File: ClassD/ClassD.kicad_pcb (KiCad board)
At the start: 2 copper layers, 53 parts, among them P1 RedRCA, P2 WhiteRCA, P3 CONN_01X02, P4 CONN_01X02, P5 CONN_01X02, SW1 SW_PUSH, SW2 SW_PUSH, U1 TDA7491LP, U2 MCP1700T

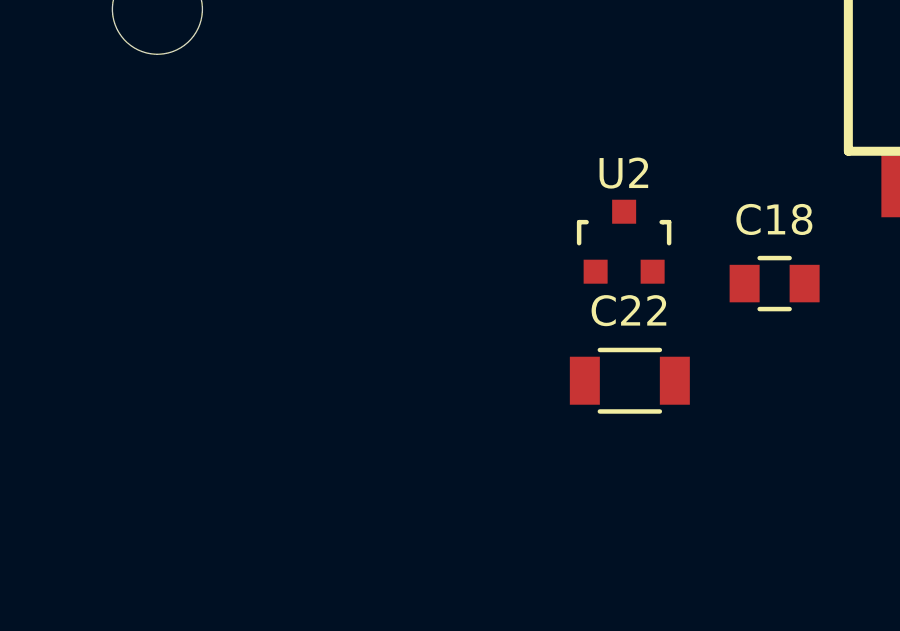
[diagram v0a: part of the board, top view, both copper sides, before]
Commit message: Added power indicator LED
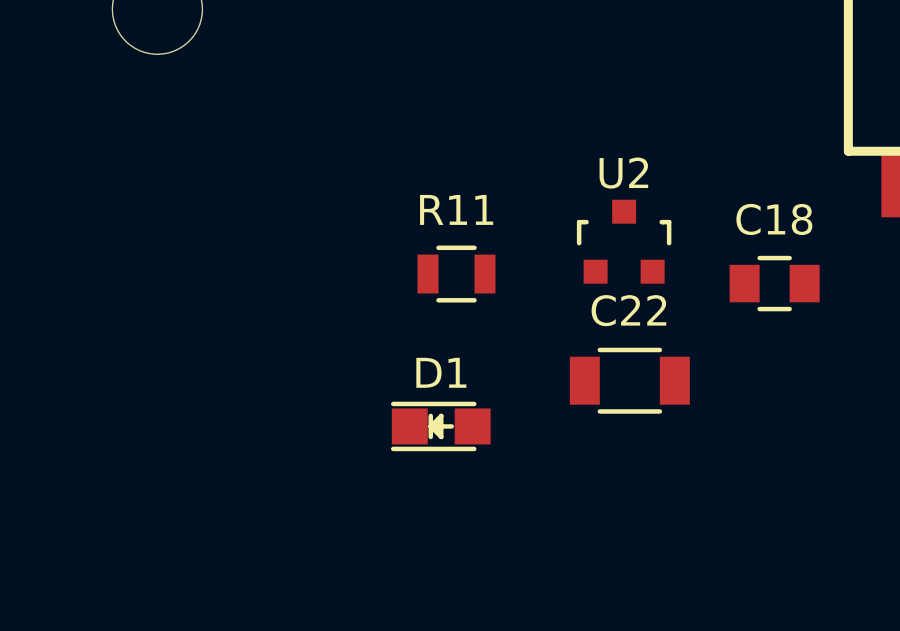
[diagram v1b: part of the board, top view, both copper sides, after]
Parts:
- added D1: LED, LEDs:LED_0805, F.Cu at (140.7, 160.4)
- added R11: 499, Resistors_SMD:R_0805, F.Cu at (141.2, 155.3)
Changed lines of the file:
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@@
 (kicad_pcb (version 4) (host pcbnew 4.0.1-3.201512221402+6198~38~ubuntu14.04.1-stable)
   (general
-    (links 110)
-    (no_connects 110)
-    (area 0 0 0 0)
+    (links 113)
+    (no_connects 113)
+    (area -2.125001 -3.225 273.562881 166.4065)
     (thickness 1.6)
     (drawings 0)
     (tracks 0)
     (zones 0)
-    (modules 53)
-    (nets 39)
+    (modules 55)
+    (nets 40)
   )
   (page A4)
@@
   (net 37 "Net-(R7-Pad2)")
   (net 38 "Net-(R8-Pad2)")
+  (net 39 "Net-(D1-Pad1)")
   (net_class Default "This is the default net class."
     (clearance 0.2)
@@
     (add_net "Net-(C6-Pad1)")
     (add_net "Net-(C9-Pad2)")
+    (add_net "Net-(D1-Pad1)")
     (add_net "Net-(L1-Pad2)")
     (add_net "Net-(L3-Pad2)")
@@
       (at (xyz 0 0 0))
       (scale (xyz 1 1 1))
+      (rotate (xyz 0 0 0))
+    )
+  )
+  (module LEDs:LED_0805 (layer F.Cu)
+    (at 140.6525 160.401)
+    (descr "LED 0805 smd package")
+    (tags "LED 0805 SMD")
+    (attr smd)
+    (fp_text reference D1 (at 0 -1.75) (layer F.SilkS)
+      (effects (font (size 1 1) (thickness 0.15)))
+    )
+    (fp_text value LED (at 0 1.75) (layer F.Fab)
+      (effects (font (size 1 1) (thickness 0.15)))
+    )
+    (fp_line (start -1.6 0.75) (end 1.1 0.75) (layer F.SilkS) (width 0.15))
+    (fp_line (start -1.6 -0.75) (end 1.1 -0.75) (layer F.SilkS) (width 0.15))
+    (fp_line (start -0.1 0.15) (end -0.1 -0.1) (layer F.SilkS) (width 0.15))
+    (fp_line (start -0.1 -0.1) (end -0.25 0.05) (layer F.SilkS) (width 0.15))
+    (fp_line (start -0.35 -0.35) (end -0.35 0.35) (layer F.SilkS) (width 0.15))
+    (fp_line (start 0 0) (end 0.35 0) (layer F.SilkS) (width 0.15))
+    (fp_line (start -0.35 0) (end 0 -0.35) (layer F.SilkS) (width 0.15))
+    (fp_line (start 0 -0.35) (end 0 0.35) (layer F.SilkS) (width 0.15))
+    (fp_line (start 0 0.35) (end -0.35 0) (layer F.SilkS) (width 0.15))
+    (fp_line (start 1.9 -0.95) (end 1.9 0.95) (layer F.CrtYd) (width 0.05))
+    (fp_line (start 1.9 0.95) (end -1.9 0.95) (layer F.CrtYd) (width 0.05))
+    (fp_line (start -1.9 0.95) (end -1.9 -0.95) (layer F.CrtYd) (width 0.05))
+    (fp_line (start -1.9 -0.95) (end 1.9 -0.95) (layer F.CrtYd) (width 0.05))
+    (pad 2 smd rect (at 1.04902 0 180) (size 1.19888 1.19888) (layers F.Cu F.Paste F.Mask)
+      (net 26 /3V3))
+    (pad 1 smd rect (at -1.04902 0 180) (size 1.19888 1.19888) (layers F.Cu F.Paste F.Mask)
+      (net 39 "Net-(D1-Pad1)"))
+    (model LEDs.3dshapes/LED_0805.wrl
+      (at (xyz 0 0 0))
+      (scale (xyz 1 1 1))
+      (rotate (xyz 0 0 0))
+    )
+  )
+  (module Resistors_SMD:R_0805 (layer F.Cu)
+    (at 141.1605 155.321)
+    (descr "Resistor SMD 0805, reflow soldering, Vishay (see dcrcw.pdf)")
+    (tags "resistor 0805")
+    (attr smd)
+    (fp_text reference R11 (at 0 -2.1) (layer F.SilkS)
+      (effects (font (size 1 1) (thickness 0.15)))
+    )
+    (fp_text value 499 (at 0 2.1) (layer F.Fab)
+      (effects (font (size 1 1) (thickness 0.15)))
+    )
+    (fp_line (start -1.6 -1) (end 1.6 -1) (layer F.CrtYd) (width 0.05))
+    (fp_line (start -1.6 1) (end 1.6 1) (layer F.CrtYd) (width 0.05))
+    (fp_line (start -1.6 -1) (end -1.6 1) (layer F.CrtYd) (width 0.05))
+    (fp_line (start 1.6 -1) (end 1.6 1) (layer F.CrtYd) (width 0.05))
+    (fp_line (start 0.6 0.875) (end -0.6 0.875) (layer F.SilkS) (width 0.15))
+    (fp_line (start -0.6 -0.875) (end 0.6 -0.875) (layer F.SilkS) (width 0.15))
+    (pad 1 smd rect (at -0.95 0) (size 0.7 1.3) (layers F.Cu F.Paste F.Mask)
+      (net 39 "Net-(D1-Pad1)"))
+    (pad 2 smd rect (at 0.95 0) (size 0.7 1.3) (layers F.Cu F.Paste F.Mask)
+      (net 5 OGND))
+    (model Resistors_SMD.3dshapes/R_0805.wrl
+      (at (xyz 0 0 0))
+      (scale (xyz 1 1 1))

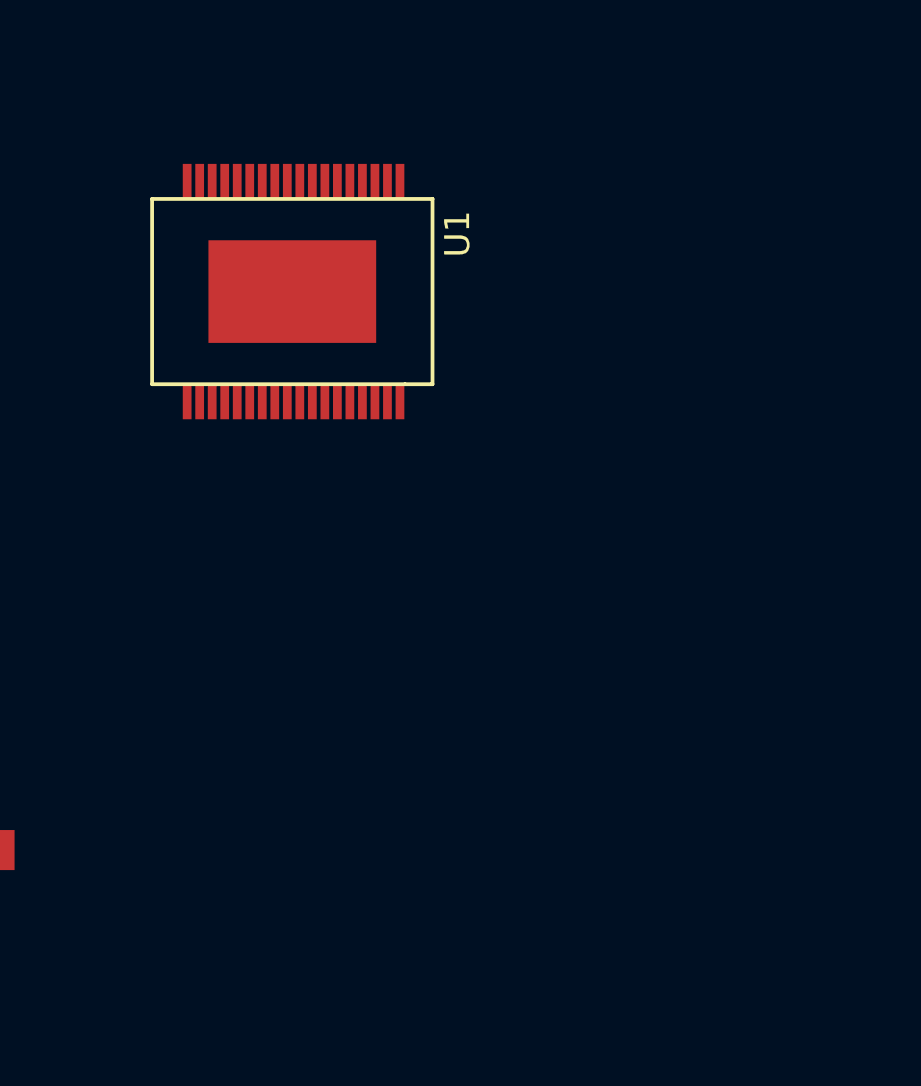
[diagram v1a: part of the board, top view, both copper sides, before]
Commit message: Added ferrites, finished component grouping
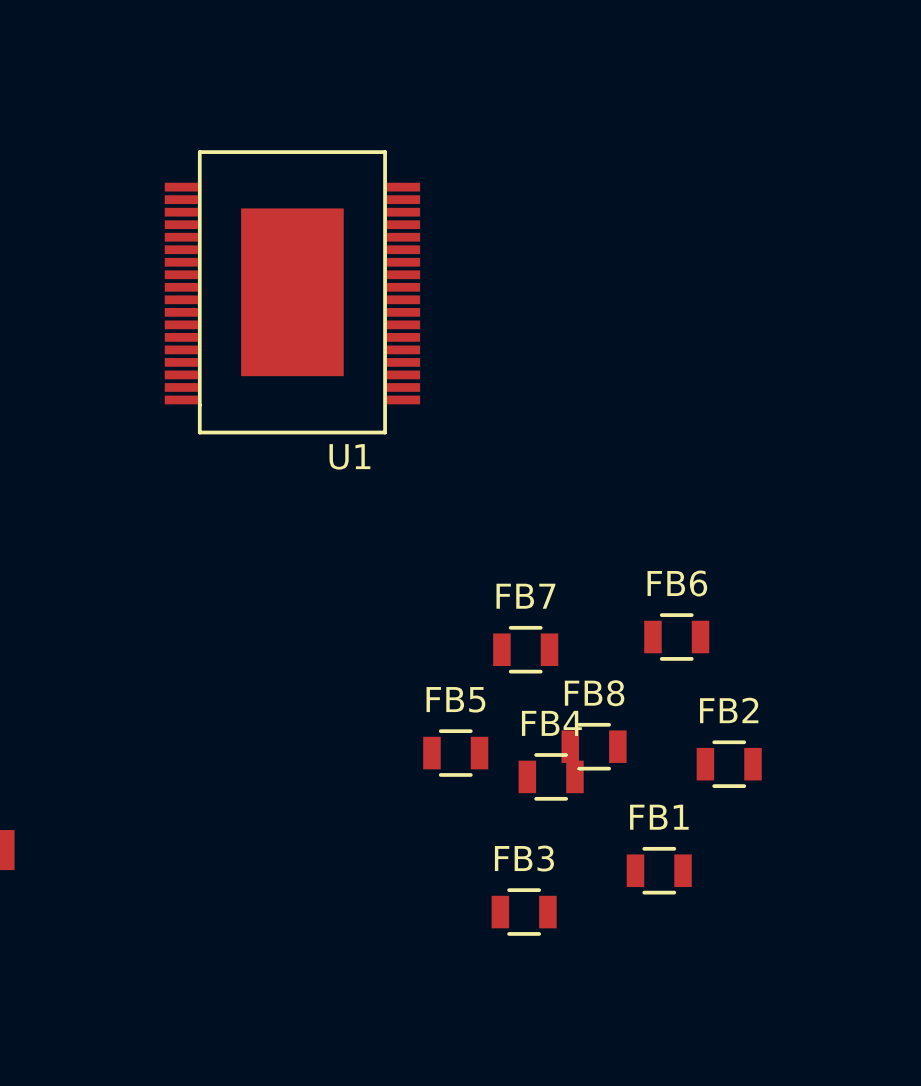
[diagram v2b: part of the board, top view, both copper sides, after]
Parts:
- added FB1: Ferrite, Resistors_SMD:R_0805, F.Cu at (193.6, 140.3)
- added FB2: Ferrite, Resistors_SMD:R_0805, F.Cu at (196.4, 136.0)
- added FB3: Ferrite, Resistors_SMD:R_0805, F.Cu at (188.2, 141.9)
- added FB4: Ferrite, Resistors_SMD:R_0805, F.Cu at (189.3, 136.5)
- added FB5: Ferrite, Resistors_SMD:R_0805, F.Cu at (185.5, 135.6)
- added FB6: Ferrite, Resistors_SMD:R_0805, F.Cu at (194.3, 130.9)
- added FB7: Ferrite, Resistors_SMD:R_0805, F.Cu at (188.3, 131.4)
- added FB8: Ferrite, Resistors_SMD:R_0805, F.Cu at (191.0, 135.3)
- moved U1 9.46 mm to (175.3, 111.6), turned to 0 degrees
